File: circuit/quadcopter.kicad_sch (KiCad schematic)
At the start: 116 parts, among them J1 Conn_01x01_Female, J10 Conn_01x01_Female, J13 Conn_01x01_Female, J15 Conn_01x01_Female, J16 Conn_01x01_Female, J17 Conn_01x01_Female, J18 USB_C_Receptacle_USB2.0, J19 Conn_01x08_Male, J2 Conn_01x01_Female, J21 Conn_01x01_Female, J22 Conn_01x01_Female, J23 Conn_01x01_Female, J24 Conn_01x01_Female, J25 Conn_01x01_Female, J26 Conn_01x01_Female, J28 Conn_01x01_Female, J29 Conn_01x01_Female, J3 Conn_01x01_Female, J30 Conn_01x01_Female, J31 Conn_01x01_Female, J32 Conn_01x01_Female, J33 Conn_01x01_Female, J34 Conn_01x01_Female, J37 Conn_01x01_Female, J4 Conn_01x01_Female, J40 Conn_01x01_Female, J41 Conn_01x01_Female, J42 Conn_01x01_Female, J43 Conn_01x01_Female, J44 Conn_01x01_Female, J45 Conn_01x01_Female, J46 Conn_01x01_Female, J47 Conn_01x01_Female, J48 Conn_01x01_Female, J49 Conn_01x01_Female, J5 Conn_Coaxial, J50 Conn_01x01_Female, J6 Conn_01x06_Male, J7 Conn_01x01_Female, J8 Conn_01x01_Female, J9 Conn_01x01_Female, Q1 AO3400A, SW1 SW_DIP_x01, U1 STM32G431CBU6, U2 ICM-42605, U3 DPS310, U4 3V3, U5 5V out, 30V max, U7 W25Q80DVUXIE TR, U8 SX1281, Y1 16M, Y2 52Mhz

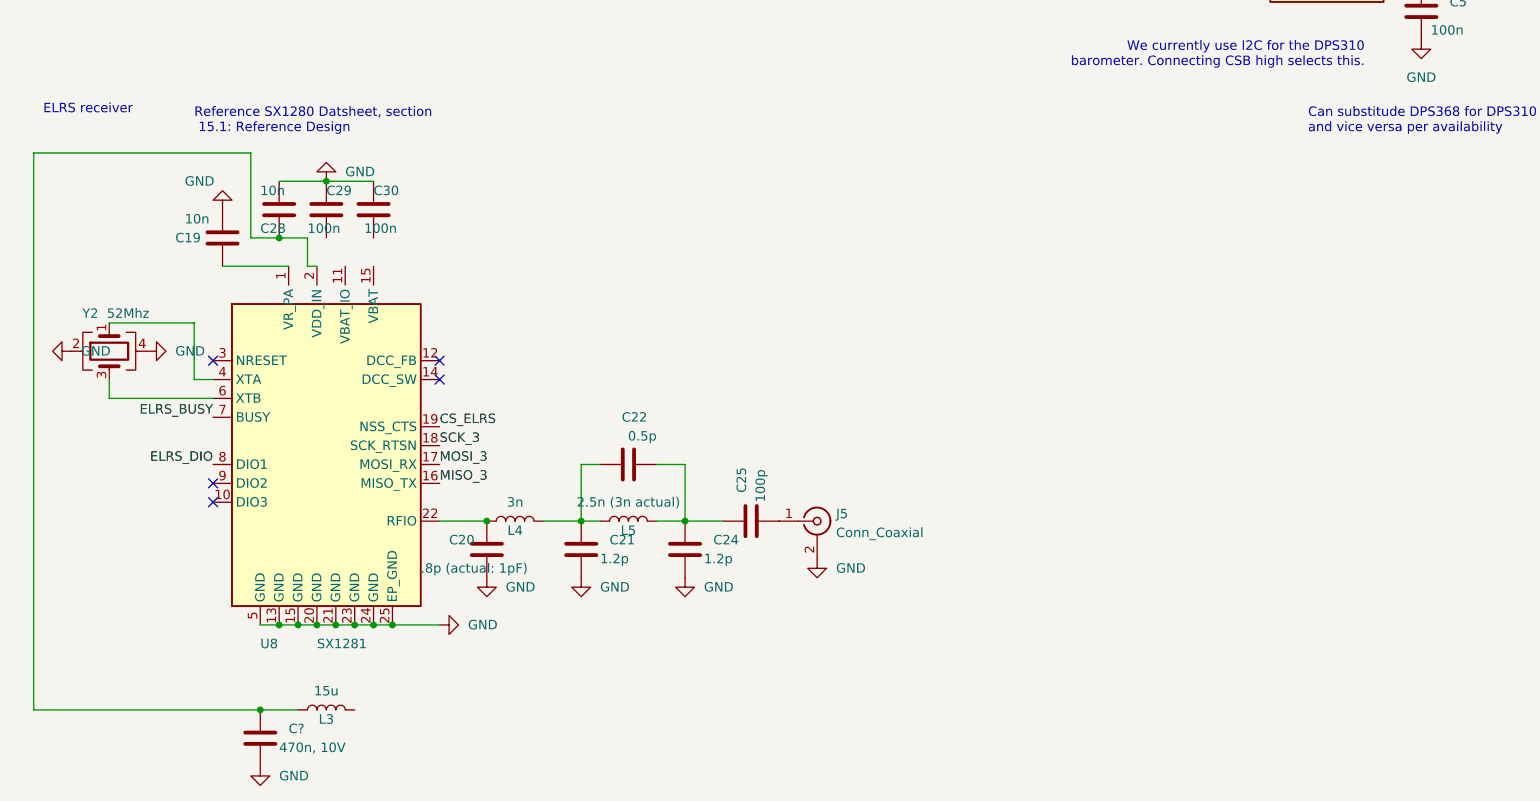
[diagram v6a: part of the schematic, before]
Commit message: replaced passive filter on RF with single IC
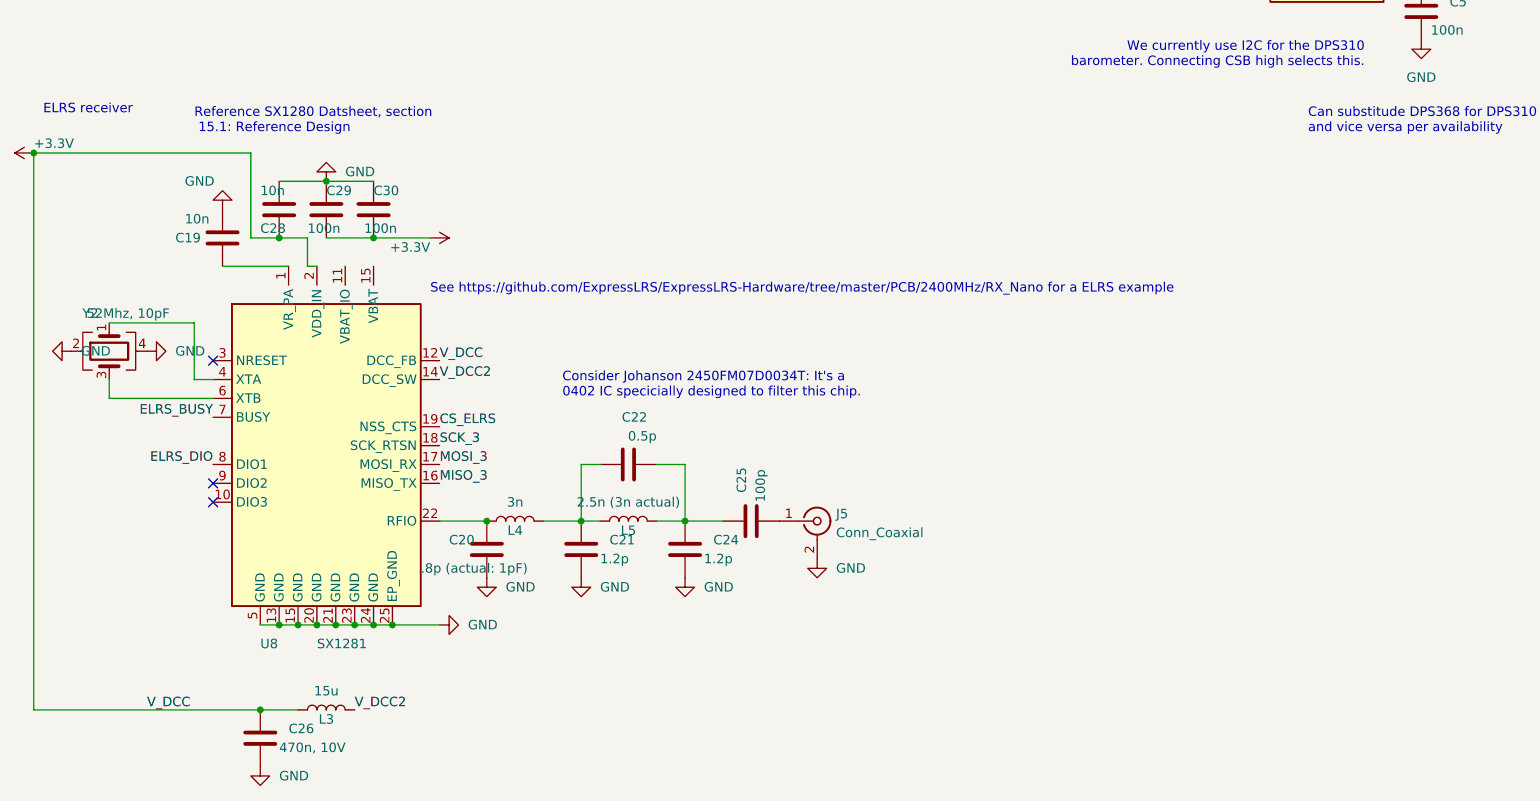
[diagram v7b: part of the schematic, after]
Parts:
- Y2: value 52Mhz -> 52Mhz, 10pF; footprint Crystal:Crystal_SMD_2016-4Pin_2.0x1.6mm -> Crystal:Crystal_SMD_3225-4Pin_3.2x2.5mm; Digikey (none) -> 2388-SXT32410AA07-52.000MT-ND; LCSC C254300 -> (none)
- gave numbers to parts that had none: 1
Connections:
- net +3V3: now also C26.1, C28.2, C29.2, C30.2, L3.1, U8.12 (DCC_FB), U8.2 (VDD_IN)
- net V_DCC2: now reaches L3.2
- net V_DCC2: now also U8.14 (DCC_SW)
- no-connect marks 9 -> 7
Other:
- note added: "Consider Johanson 2450FM07D0034T: It's a 0402 IC specicially designed to filter this chip."
- note added: "See https://github.com/ExpressLRS/ExpressLRS-Hardware/tree/master/PCB/2400MHz/RX_Nano for a ELRS example"
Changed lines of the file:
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@@
   (junction (at 132.08 48.26) (diameter 0) (color 0 0 0 0)
   )
+  (junction (at 69.85 273.05) (diameter 0) (color 0 0 0 0)
+  )
   (junction (at 100.33 76.2) (diameter 0) (color 0 0 0 0)
   )
   (junction (at 58.42 130.81) (diameter 0) (color 0 0 0 0)
   )
+  (junction (at 24.13 261.62) (diameter 0) (color 0 0 0 0)
+  )
   (junction (at 210.82 231.14) (diameter 0) (color 0 0 0 0)
   )
@@
   (no_connect (at 48.26 289.56))
   (no_connect (at 48.26 308.61))
-  (no_connect (at 78.74 289.56))
-  (no_connect (at 78.74 292.1))
   (no_connect (at 48.26 306.07))
   (no_connect (at 27.94 231.14))
@@
     (stroke (width 0) (type default) (color 0 0 0 0))
   )
+  (wire (pts (xy 63.5 273.05) (xy 69.85 273.05))
+    (stroke (width 0) (type default) (color 0 0 0 0))
+  )
   (wire (pts (xy 110.49 34.29) (xy 116.84 34.29))
     (stroke (width 0) (type default) (color 0 0 0 0))
@@
     (stroke (width 0) (type default) (color 0 0 0 0))
   )
+  (wire (pts (xy 69.85 273.05) (xy 77.47 273.05))
+    (stroke (width 0) (type default) (color 0 0 0 0))
+  )
   (wire (pts (xy 63.5 265.43) (xy 69.85 265.43))
     (stroke (width 0) (type default) (color 0 0 0 0))
@@
     (effects (font (size 1.27 1.27)) (justify left bottom))
   )
+  (text "Consider Johanson 2450FM07D0034T: It's a \n0402 IC specicially designed to filter this chip."
+    (at 95.25 294.64 0)
+    (effects (font (size 1.27 1.27)) (justify left bottom))
+  )
   (text "5v on USART lines?\n" (at 80.01 152.4 0)
     (effects (font (size 1.27 1.27)) (justify left bottom))
@@
     (effects (font (size 1.27 1.27)) (justify left bottom))
   )
+  (text "See https://github.com/ExpressLRS/ExpressLRS-Hardware/tree/master/PCB/2400MHz/RX_Nano for a ELRS example"
+    (at 77.47 280.67 0)
+    (effects (font (size 1.27 1.27)) (justify left bottom))
+  )
   (text "Ground pin 2 for ISM330 compatibility.\nDoesn't matter for ICM42605\n"
     (at 189.23 153.67 0)
@@
     (effects (font (size 1.27 1.27)) (justify left bottom))
   )
+  (label "V_DCC2" (at 67.31 336.55 0)
+    (effects (font (size 1.27 1.27)) (justify left bottom))
+  )
   (label "M2" (at 113.03 104.14 180)
     (effects (font (size 1.27 1.27)) (justify right bottom))
@@
     (effects (font (size 1.27 1.27)) (justify left bottom))
   )
+  (label "V_DCC" (at 39.37 336.55 0)
+    (effects (font (size 1.27 1.27)) (justify left bottom))
+  )
   (label "CURRENT" (at 422.91 33.02 180)
     (effects (font (size 1.27 1.27)) (justify right bottom))
@@
     (effects (font (size 1.27 1.27)) (justify right bottom))
   )
+  (label "V_DCC2" (at 78.74 292.1 0)
+    (effects (font (size 1.27 1.27)) (justify left bottom))
+  )
   (label "UART1_TX" (at 375.92 257.81 180)
     (effects (font (size 1.27 1.27)) (justify right bottom))
@@
     (effects (font (size 1.27 1.27)) (justify right bottom))
   )
+  (label "V_DCC" (at 78.74 289.56 0)
+    (effects (font (size 1.27 1.27)) (justify left bottom))
+  )
   (label "BOOT0" (at 143.51 81.28 0)
     (effects (font (size 1.27 1.27)) (justify left bottom))
@@
   (symbol (lib_id "power:GND") (at 54.61 344.17 0) (unit 1)
     (in_bom yes) (on_board yes) (fields_autoplaced)
-    (property "Reference" "#PWR?" (id 0) (at 54.61 350.52 0)
+    (property "Reference" "#PWR0153" (id 0) (at 54.61 350.52 0)
       (effects (font (size 1.27 1.27)) hide)
     )
@@
   (symbol (lib_id "Device:C") (at 54.61 340.36 0) (unit 1)
     (in_bom yes) (on_board yes)
-    (property "Reference" "C?" (id 0) (at 58.42 339.0899 0)
+    (property "Reference" "C26" (id 0) (at 58.42 339.0899 0)
       (effects (font (size 1.27 1.27)) (justify left))
     )
@@
     (pin "1")
   )
+  (symbol (lib_id "power:+3.3V") (at 77.47 273.05 270) (unit 1)
+    (in_bom yes) (on_board yes)
+    (property "Reference" "#PWR0155" (id 0) (at 73.66 273.05 0)
+      (effects (font (size 1.27 1.27)) hide)
+    )
+    (property "Value" "+3.3V" (id 1) (at 77.47 274.32 90)
+      (effects (font (size 1.27 1.27)) (justify right))
+    )
+    (property "Footprint" "" (id 2) (at 77.47 273.05 0)
+      (effects (font (size 1.27 1.27)) hide)
+    )
+    (property "Datasheet" "" (id 3) (at 77.47 273.05 0)
+      (effects (font (size 1.27 1.27)) hide)
+    )
+    (pin "1")
+  )
   (symbol (lib_id "Connector:Conn_01x01_Female") (at 394.97 96.52 0) (unit 1)
     (in_bom yes) (on_board yes) (fields_autoplaced)
@@
     (pin "2")
   )
+  (symbol (lib_id "power:+3.3V") (at 24.13 261.62 90) (unit 1)
+    (in_bom yes) (on_board yes)
+    (property "Reference" "#PWR0154" (id 0) (at 27.94 261.62 0)
+      (effects (font (size 1.27 1.27)) hide)
+    )
+    (property "Value" "+3.3V" (id 1) (at 24.13 260.35 90)
+      (effects (font (size 1.27 1.27)) (justify right))
+    )
+    (property "Footprint" "" (id 2) (at 24.13 261.62 0)
+      (effects (font (size 1.27 1.27)) hide)
+    )
+    (property "Datasheet" "" (id 3) (at 24.13 261.62 0)
+      (effects (font (size 1.27 1.27)) hide)
+    )
+    (pin "1")
+  )
   (symbol (lib_id "Mechanical:MountingHole") (at 279.4 127 0) (unit 1)
     (in_bom yes) (on_board yes) (fields_autoplaced)
@@
     (in_bom yes) (on_board yes)
     (property "Reference" "Y2" (id 0) (at 31.75 283.21 90))
-    (property "Value" "52Mhz" (id 1) (at 36.83 283.21 90))
-    (property "Footprint" "Crystal:Crystal_SMD_2016-4Pin_2.0x1.6mm" (id 2) (at 34.29 288.29 0)
+    (property "Value" "52Mhz, 10pF" (id 1) (at 36.83 283.21 90))
+    (property "Footprint" "Crystal:Crystal_SMD_3225-4Pin_3.2x2.5mm" (id 2) (at 34.29 288.29 0)
+      (effects (font (size 1.27 1.27)) hide)
+    )
+    (property "Datasheet" "https://suntsu.com/wp-content/uploads/2020/07/SXT324-Series-1.pdf" (id 3) (at 34.29 288.29 0)
       (effects (font (size 1.27 1.27)) hide)
     )
-    (property "Datasheet" "https://datasheet.lcsc.com/lcsc/1912111437_HELE-Harmony-Elec-X2C016000B81H-R_C254300.pdf" (id 3) (at 34.29 288.29 0)
+    (property "LCSC" "" (id 4) (at 34.29 288.29 0)
       (effects (font (size 1.27 1.27)) hide)
     )
-    (property "LCSC" "C254300" (id 4) (at 34.29 288.29 0)
+    (property "Digikey" "2388-SXT32410AA07-52.000MT-ND" (id 5) (at 34.29 288.29 90)
       (effects (font (size 1.27 1.27)) hide)
     )
@@
       (reference "#PWR0152") (unit 1) (value "GND") (footprint "")
     )
+    (path "/25499ee9-681f-42ea-87da-03718de06b1e"
+      (reference "#PWR0153") (unit 1) (value "GND") (footprint "")
+    )
+    (path "/b7ef3f82-e9f8-4798-80c9-68d70eba13ec"
+      (reference "#PWR0154") (unit 1) (value "+3.3V") (footprint "")
+    )
+    (path "/7e00f2a1-3211-48eb-9668-06ca271de0c1"
+      (reference "#PWR0155") (unit 1) (value "+3.3V") (footprint "")
+    )
     (path "/84b179b0-80ba-4331-8f2d-2245c4bebdf5"
       (reference "#PWR0156") (unit 1) (value "+3.3V") (footprint "")
@@
       (reference "#PWR0178") (unit 1) (value "GND") (footprint "")
     )
-    (path "/25499ee9-681f-42ea-87da-03718de06b1e"
-      (reference "#PWR?") (unit 1) (value "GND") (footprint "")
-    )
     (path "/4392ec2f-3eec-47ea-978d-f1725d990b74"
       (reference "C1") (unit 1) (value "2.2u") (footprint "Capacitor_SMD:C_0402_1005Metric")
@@
       (reference "C25") (unit 1) (value "100p") (footprint "Capacitor_SMD:C_0402_1005Metric")
     )
+    (path "/39ccf20f-79e3-4513-994e-00a92108452e"
+      (reference "C26") (unit 1) (value "470n, 10V") (footprint "Capacitor_SMD:C_0402_1005Metric")
+    )
     (path "/f52e9835-147d-4eea-ab24-2abbf0cd1a27"
       (reference "C27") (unit 1) (value "22u 35v") (footprint "Capacitor_SMD:C_0805_2012Metric")
@@
       (reference "C31") (unit 1) (value "100u") (footprint "Capacitor_SMD:C_0805_2012Metric")
     )
-    (path "/39ccf20f-79e3-4513-994e-00a92108452e"
-      (reference "C?") (unit 1) (value "470n, 10V") (footprint "Capacitor_SMD:C_0402_1005Metric")
-    )
     (path "/ee5b5e6d-6153-4553-b0e5-378d0575119f"
       (reference "D1") (unit 1) (value "40v 1A B5819WS") (footprint "Diode_SMD:D_SOD-323")
@@
     )
     (path "/d55c58ae-9adf-4d6c-b50f-1f7069002113"
-      (reference "Y2") (unit 1) (value "52Mhz") (footprint "Crystal:Crystal_SMD_2016-4Pin_2.0x1.6mm")
+      (reference "Y2") (unit 1) (value "52Mhz, 10pF") (footprint "Crystal:Crystal_SMD_3225-4Pin_3.2x2.5mm")
     )
   )

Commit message: Adjusted connections and routing for ELRS power system
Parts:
- removed C20: .8p (actual: 1pF), Capacitor_SMD:C_0402_1005Metric, symbol Device:C
- removed C21, C24: 1.2p, Capacitor_SMD:C_0402_1005Metric, symbol Device:C
- removed C22: 0.5p, Capacitor_SMD:C_0402_1005Metric, symbol Device:C
- removed C25: 100p, Capacitor_SMD:C_0402_1005Metric, symbol Device:C
- removed L4: 3n, Inductor_SMD:L_0402_1005Metric, symbol Device:L
- removed L5: 2.5n (3n actual), Inductor_SMD:L_0402_1005Metric, symbol Device:L
- added U6: 2450FM07D0034T, Anyleaf_Shared:2450FM07D0034, symbol Filter:SAFFA1G58KA0F0A
- Y2: value 52Mhz, 10pF -> 52Mhz, 12pF; footprint Crystal:Crystal_SMD_3225-4Pin_3.2x2.5mm -> Crystal:Crystal_SMD_2016-4Pin_2.0x1.6mm; Digikey 2388-SXT32410AA07-52.000MT-ND -> FL520WFMT1TR-ND; Mouser (none) -> 729-FW520WFMT1
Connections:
- net +3V3: now also C19.2, U8.1 (VR_PA), U8.11 (VBAT_IO), U8.15 (VBAT); no longer U8.12 (DCC_FB)
- net GND: now also U6.2, U6.4, U6.5
- net UART1_RX: now also J4.1 (Pin_1), J6.1 (Pin_1); no longer J28.1 (Pin_1), J6.3 (Pin_3)
- net UART1_TX: no longer J13.1 (Pin_1), J6.4 (Pin_4)
- net UART2_RX: now also J28.1 (Pin_1), J6.3 (Pin_3); no longer J43.1 (Pin_1), J6.1 (Pin_1)
- net UART2_TX: now also J13.1 (Pin_1), J6.4 (Pin_4); no longer J4.1 (Pin_1), J42.1 (Pin_1)
- net UART4_RX: now also J43.1 (Pin_1)
- net UART4_TX: now also J42.1 (Pin_1)
- net at U8.22 (RFIO): now also U6.1
- net at J5.1 (In): now also U6.3
- new net V_DCC: U8.12 (DCC_FB)
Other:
- note added: "(HDL / SA)"
- note added: "Note: DJI uses optional HDL (SBUS), which is Rx. HDzero uses optional Smart Audio, which is Tx. So, you have a choice"
- note added: "On PCB, position pad 1 of filter 0.15mm from RFIO pad on SX1280, lined up with it - per filter DS."
- note removed: "(HDL / SBUS)"
- moved on the sheet: J5
